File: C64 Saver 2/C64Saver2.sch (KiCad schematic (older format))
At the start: 20 parts, among them J1 Conn_01x04, J2 Conn_01x08, J4 Conn_01x08, J5 Conn_01x04, J6 Conn_01x04, Q1 2N7000, Q2 IRFR5305

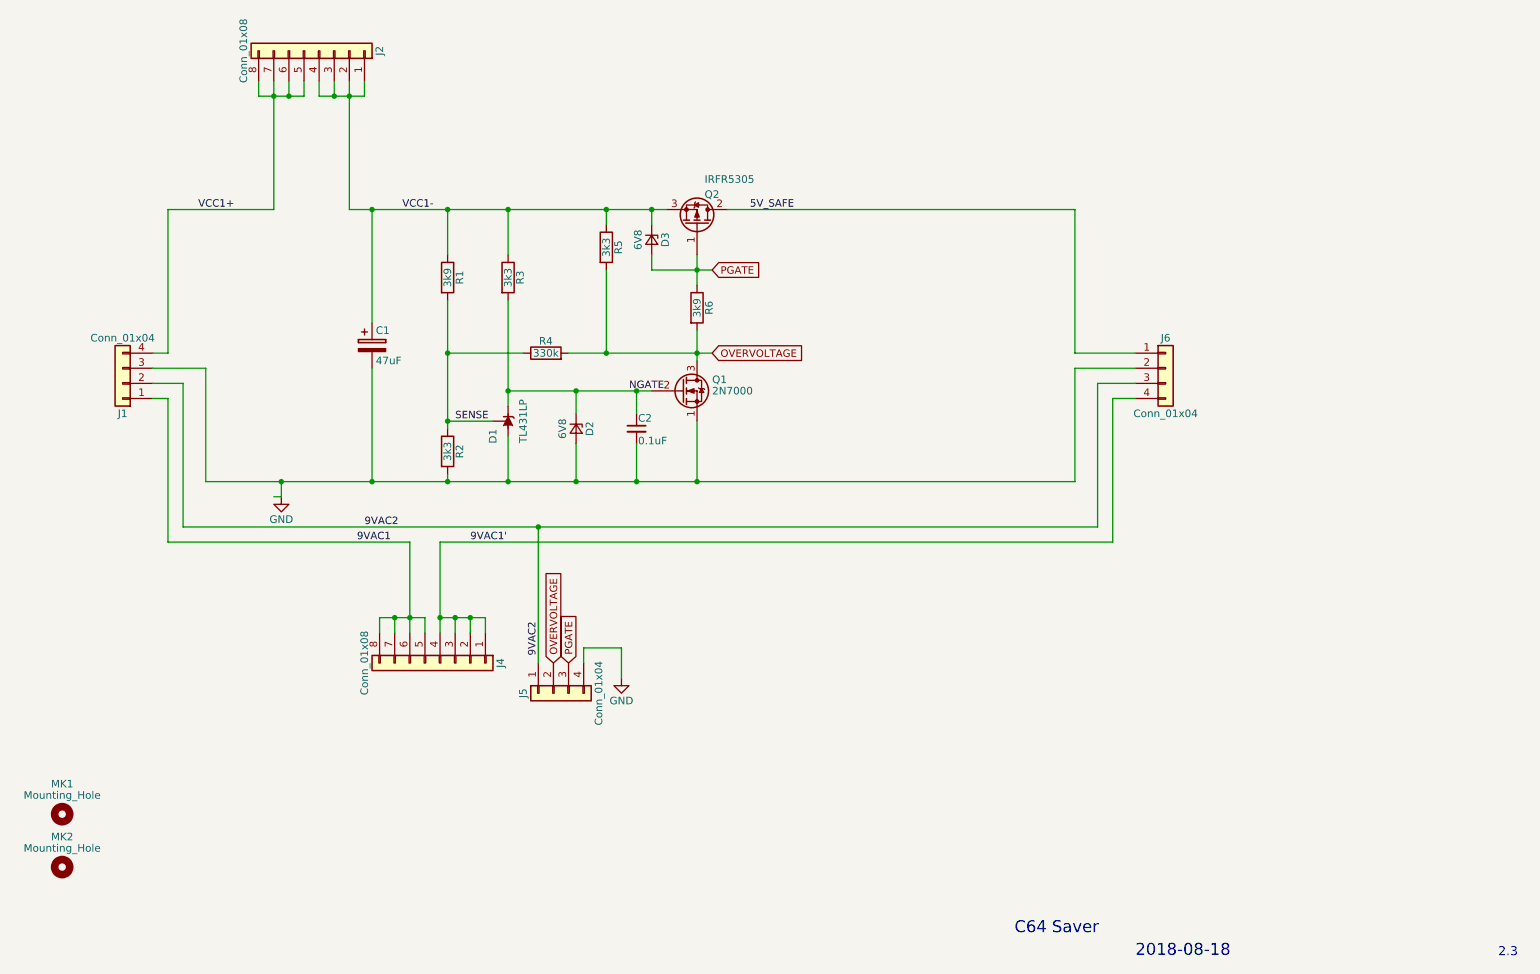
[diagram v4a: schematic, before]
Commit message: New layout new routing. Resistor divider to support low Vth. #13
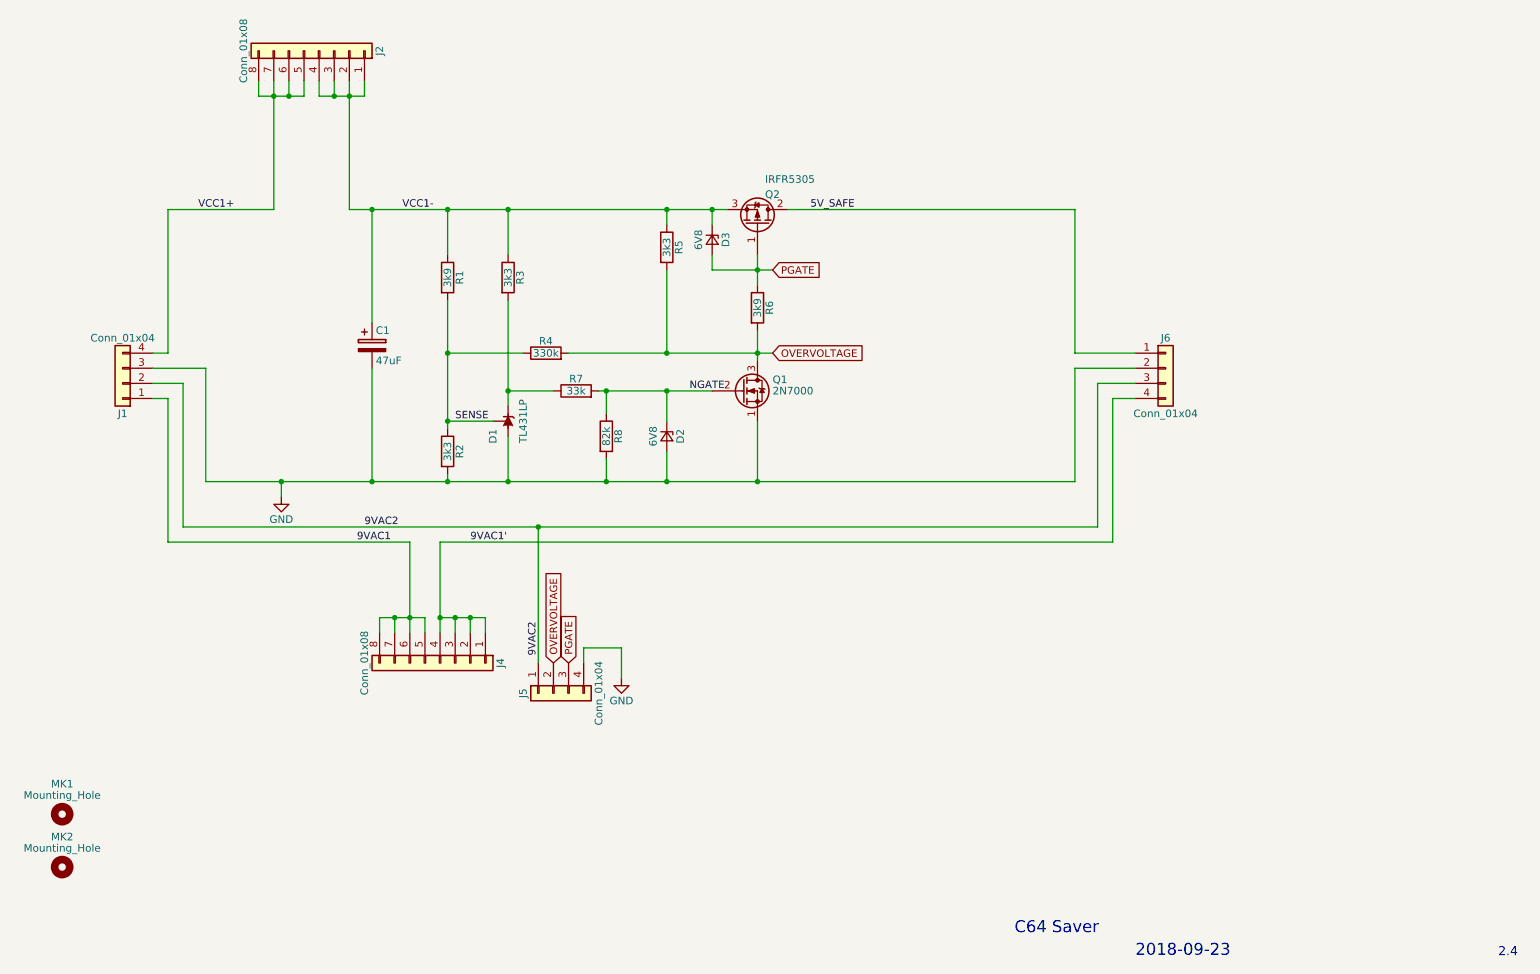
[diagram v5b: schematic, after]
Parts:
- removed C2: 0.1uF, Capacitors_THT:C_Disc_D3.8mm_W2.6mm_P2.50mm, symbol C_Small
- added R7: 33k, Resistors_THT:R_Axial_DIN0204_L3.6mm_D1.6mm_P5.08mm_Horizontal, symbol R
- added R8: 82k, Resistors_THT:R_Axial_DIN0204_L3.6mm_D1.6mm_P5.08mm_Horizontal, symbol R
- Q1: footprint TO_SOT_Packages_THT:TO-92_Molded_Narrow -> TO_SOT_Packages_THT:TO-92_Inline_Wide
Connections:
- net GND: now also R8.2
- net NGATE: now also R7.2, R8.1; no longer D1.3 (K), R3.2
- new net: D1.3 (K), R3.2, R7.1
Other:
- note added: "2.4"
- note added: "2018-09-23"
- note removed: "2.3"
- note removed: "2018-08-18"
- moved on the sheet: D2, D3, Q1, Q2, R5, R6
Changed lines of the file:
@@
 L D_Zener_Small D2
 U 1 1 5B1D3C9A
-P 4500 4150
-F 0 "D2" H 4500 4240 50  0000 C CNN
-F 1 "6V8" H 4500 4060 50  0000 C CNN
-F 2 "Diodes_THT:D_DO-35_SOD27_P7.62mm_Horizontal" V 4500 4150 50  0001 C CNN
-F 3 "" V 4500 4150 50  0001 C CNN
-	1    4500 4150
+P 5100 4200
+F 0 "D2" H 5100 4290 50  0000 C CNN
+F 1 "6V8" H 5100 4110 50  0000 C CNN
+F 2 "Diodes_THT:D_DO-35_SOD27_P7.62mm_Horizontal" V 5100 4200 50  0001 C CNN
+F 3 "" V 5100 4200 50  0001 C CNN
+	1    5100 4200
 	0    1    1    0
 $EndComp
@@
 $EndComp
 $Comp
-L C_Small C2
-U 1 1 5B1D7082
-P 4900 4150
-F 0 "C2" H 4910 4220 50  0000 L CNN
-F 1 "0.1uF" H 4910 4070 50  0000 L CNN
-F 2 "Capacitors_THT:C_Disc_D3.8mm_W2.6mm_P2.50mm" H 4900 4150 50  0001 C CNN
-F 3 "" H 4900 4150 50  0001 C CNN
-	1    4900 4150
-	1    0    0    -1
-$EndComp
-$Comp
 L R R6
 U 1 1 5B1D73D7
-P 5300 3350
-F 0 "R6" V 5380 3350 50  0000 C CNN
-F 1 "3k9" V 5300 3350 50  0000 C CNN
-F 2 "Resistors_THT:R_Axial_DIN0204_L3.6mm_D1.6mm_P5.08mm_Horizontal" V 5230 3350 50  0001 C CNN
-F 3 "" H 5300 3350 50  0001 C CNN
-	1    5300 3350
+P 5700 3350
+F 0 "R6" V 5780 3350 50  0000 C CNN
+F 1 "3k9" V 5700 3350 50  0000 C CNN
+F 2 "Resistors_THT:R_Axial_DIN0204_L3.6mm_D1.6mm_P5.08mm_Horizontal" V 5630 3350 50  0001 C CNN
+F 3 "" H 5700 3350 50  0001 C CNN
+	1    5700 3350
 	1    0    0    -1
 $EndComp
@@
 L R R5
 U 1 1 5B1D747E
-P 4700 2950
-F 0 "R5" V 4780 2950 50  0000 C CNN
-F 1 "3k3" V 4700 2950 50  0000 C CNN
-F 2 "Resistors_THT:R_Axial_DIN0204_L3.6mm_D1.6mm_P5.08mm_Horizontal" V 4630 2950 50  0001 C CNN
-F 3 "" H 4700 2950 50  0001 C CNN
-	1    4700 2950
+P 5100 2950
+F 0 "R5" V 5180 2950 50  0000 C CNN
+F 1 "3k3" V 5100 2950 50  0000 C CNN
+F 2 "Resistors_THT:R_Axial_DIN0204_L3.6mm_D1.6mm_P5.08mm_Horizontal" V 5030 2950 50  0001 C CNN
+F 3 "" H 5100 2950 50  0001 C CNN
+	1    5100 2950
 	1    0    0    -1
 $EndComp
@@
 L D_Zener_Small D3
 U 1 1 5B1D7545
-P 5000 2900
-F 0 "D3" H 5000 2990 50  0000 C CNN
-F 1 "6V8" H 5000 2810 50  0000 C CNN
-F 2 "Diodes_THT:D_DO-35_SOD27_P7.62mm_Horizontal" V 5000 2900 50  0001 C CNN
-F 3 "" V 5000 2900 50  0001 C CNN
-	1    5000 2900
+P 5400 2900
+F 0 "D3" H 5400 2990 50  0000 C CNN
+F 1 "6V8" H 5400 2810 50  0000 C CNN
+F 2 "Diodes_THT:D_DO-35_SOD27_P7.62mm_Horizontal" V 5400 2900 50  0001 C CNN
+F 3 "" V 5400 2900 50  0001 C CNN
+	1    5400 2900
 	0    1    1    0
 $EndComp
@@
 	0    -1   -1   0
 $EndComp
-Text GLabel 5400 3100 2    49   Input ~ 0
+Text GLabel 5800 3100 2    49   Input ~ 0
 PGATE
 Text Label 3800 4900 0    49   ~ 0
@@
 Text Label 3100 4800 0    49   ~ 0
 9VAC2
-Text Label 5650 2700 0    49   ~ 0
+Text Label 6050 2700 0    49   ~ 0
 5V_SAFE
 Text Label 2000 2700 0    49   ~ 0
@@
 Text GLabel 4450 5700 1    49   Input ~ 0
 PGATE
-Text GLabel 5400 3650 2    49   Input ~ 0
+Text GLabel 5800 3650 2    49   Input ~ 0
 OVERVOLTAGE
 Text GLabel 4350 5700 1    49   Input ~ 0
@@
 Text Label 3700 4100 0    49   ~ 0
 SENSE
-Text Label 4850 3900 0    49   ~ 0
+Text Label 5250 3900 0    49   ~ 0
 NGATE
 $Comp
@@
 L Q_PMOS_GDS Q2
 U 1 1 5B217093
-P 5300 2800
-F 0 "Q2" V 5500 2850 50  0000 L CNN
-F 1 "IRFR5305" V 5600 2850 50  0000 L CNN
-F 2 "TO_SOT_Packages_SMD:ATPAK-2" H 5500 2900 50  0001 C CNN
-F 3 "" H 5300 2800 50  0001 C CNN
-	1    5300 2800
+P 5700 2800
+F 0 "Q2" V 5900 2850 50  0000 L CNN
+F 1 "IRFR5305" V 6000 2850 50  0000 L CNN
+F 2 "TO_SOT_Packages_SMD:ATPAK-2" H 5900 2900 50  0001 C CNN
+F 3 "" H 5700 2800 50  0001 C CNN
+	1    5700 2800
 	0    1    -1   0
 $EndComp
-Text Notes 10600 7650 0    60   ~ 0
-2.3
 Text Notes 7400 7500 0    79   ~ 0
 C64 Saver
 Text Notes 8200 7650 0    79   ~ 0
-2018-08-18
+2018-09-23
 Text Label 3050 4900 0    49   ~ 0
 9VAC1
@@
 	4050 4500 4050 4200
 Wire Wire Line
-	2050 4500 7800 4500
-Wire Wire Line
 	3650 4500 3650 4450
-Wire Wire Line
-	4050 3300 4050 4000
 Wire Wire Line
 	4050 2700 4050 3000
@@
 	3650 2700 3650 3000
 Connection ~ 3650 2700
-Wire Wire Line
-	4500 4050 4500 3900
-Wire Wire Line
-	4050 3900 5000 3900
-Connection ~ 4050 3900
-Wire Wire Line
-	4500 4500 4500 4250
 Connection ~ 4050 4500
-Connection ~ 4500 3900
-Wire Wire Line
-	5300 4500 5300 4100
-Connection ~ 4500 4500
-Wire Wire Line
-	4900 4050 4900 3900
-Connection ~ 4900 3900
-Wire Wire Line
-	4900 4250 4900 4500
-Connection ~ 4900 4500
-Wire Wire Line
-	5300 3500 5300 3700
+Wire Wire Line
+	5700 4500 5700 4100
+Wire Wire Line
+	5700 3500 5700 3700
 Connection ~ 4050 2700
-Connection ~ 5000 2700
-Wire Wire Line
-	5000 3000 5000 3100
-Wire Wire Line
-	4700 2700 4700 2800
-Connection ~ 4700 2700
-Wire Wire Line
-	4700 3100 4700 3650
-Connection ~ 5300 3100
-Wire Wire Line
-	4450 3650 5400 3650
-Connection ~ 5300 3650
+Connection ~ 5400 2700
+Wire Wire Line
+	5400 3000 5400 3100
+Wire Wire Line
+	5100 2700 5100 2800
+Connection ~ 5100 2700
+Wire Wire Line
+	5100 3100 5100 3650
+Connection ~ 5700 3100
+Wire Wire Line
+	4450 3650 5800 3650
+Connection ~ 5700 3650
 Wire Wire Line
 	4150 3650 3650 3650
@@
 Wire Wire Line
 	1700 3750 2050 3750
-Connection ~ 5300 4500
+Connection ~ 5700 4500
 Wire Wire Line
 	1700 3950 1800 3950
@@
 	1700 3650 1800 3650
 Wire Wire Line
-	3000 2700 5100 2700
+	3000 2700 5500 2700
 Wire Wire Line
 	1800 2700 2500 2700
-Wire Wire Line
-	2500 4600 2550 4600
 Wire Wire Line
 	2550 4600 2550 4500
 Connection ~ 2550 4500
 Wire Wire Line
-	5300 3000 5300 3200
-Wire Wire Line
-	5500 2700 7800 2700
-Wire Wire Line
-	5000 2800 5000 2700
+	5700 3000 5700 3200
+Wire Wire Line
+	5400 2800 5400 2700
 Wire Wire Line
 	3150 3450 3150 2700
@@
 Connection ~ 4250 4800
 Wire Wire Line
-	5000 3100 5400 3100
-Connection ~ 4700 3650
+	5400 3100 5800 3100
+Connection ~ 5100 3650
 $Comp
 L 2N7000 Q1
 U 1 1 5B78C547
-P 5200 3900
-F 0 "Q1" H 5400 3975 50  0000 L CNN
-F 1 "2N7000" H 5400 3900 50  0000 L CNN
-F 2 "TO_SOT_Packages_THT:TO-92_Molded_Narrow" H 5400 3825 50  0001 L CIN
-F 3 "" H 5200 3900 50  0001 L CNN
-	1    5200 3900
-	1    0    0    -1
-$EndComp
+P 5600 3900
+F 0 "Q1" H 5800 3975 50  0000 L CNN
+F 1 "2N7000" H 5800 3900 50  0000 L CNN
+F 2 "TO_SOT_Packages_THT:TO-92_Inline_Wide" H 5800 3825 50  0001 L CIN
+F 3 "" H 5600 3900 50  0001 L CNN
+	1    5600 3900
+	1    0    0    -1
+$EndComp
+Text Notes 10600 7650 0    60   ~ 0
+2.4
+Wire Wire Line
+	2050 4500 7800 4500
+$Comp
+L R R7
+U 1 1 5BA6F720
+P 4500 3900
+F 0 "R7" V 4580 3900 50  0000 C CNN
+F 1 "33k" V 4500 3900 50  0000 C CNN
+F 2 "Resistors_THT:R_Axial_DIN0204_L3.6mm_D1.6mm_P5.08mm_Horizontal" V 4430 3900 50  0001 C CNN
+F 3 "" H 4500 3900 50  0001 C CNN
+	1    4500 3900
+	0    -1   -1   0
+$EndComp
+$Comp
+L R R8
+U 1 1 5BA6F7A6
+P 4700 4200
+F 0 "R8" V 4780 4200 50  0000 C CNN
+F 1 "82k" V 4700 4200 50  0000 C CNN
+F 2 "Resistors_THT:R_Axial_DIN0204_L3.6mm_D1.6mm_P5.08mm_Horizontal" V 4630 4200 50  0001 C CNN
+F 3 "" H 4700 4200 50  0001 C CNN
+	1    4700 4200
+	1    0    0    -1
+$EndComp
+Wire Wire Line
+	4050 3300 4050 4000
+Wire Wire Line
+	4350 3900 4050 3900
+Connection ~ 4050 3900
+Wire Wire Line
+	4650 3900 5400 3900
+Wire Wire Line
+	4700 4050 4700 3900
+Connection ~ 4700 3900
+Wire Wire Line
+	4700 4350 4700 4500
+Connection ~ 4700 4500
+Wire Wire Line
+	5100 4100 5100 3900
+Connection ~ 5100 3900
+Wire Wire Line
+	5100 4300 5100 4500
+Connection ~ 5100 4500
+Wire Wire Line
+	7800 2700 5900 2700
 $EndSCHEMATC
